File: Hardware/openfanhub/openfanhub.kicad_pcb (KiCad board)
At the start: 2 copper layers, 100 x 100 mm, 110 parts, among them J1 UART, J2 I2C, J3 12V in, J4 GND in, J5 5V IN, J6 SWD, M1 Fan_4pin, M10 Fan_4pin, M11 Fan_4pin, M12 Fan_4pin, M13 Fan_4pin, M14 Fan_4pin, M15 Fan_4pin, M16 Fan_4pin, M17 Fan_4pin, M18 Fan_4pin, M2 Fan_4pin, M3 Fan_4pin, M4 Fan_4pin, M5 Fan_4pin, M6 Fan_4pin, M7 Fan_4pin, M8 Fan_4pin, M9 Fan_4pin, Q1 Q_NMOS_GSD, Q10 AO449, Q11 Q_NMOS_GSD, Q12 AO449, Q2 AO449, Q3 Q_NMOS_GSD, Q4 AO449, Q5 Q_NMOS_GSD, Q6 AO449, Q7 Q_NMOS_GSD, Q8 AO449, Q9 Q_NMOS_GSD, U1 STM32F103C8T8_Board, U2 STM32F103C8Tx, U3 AMS1117, U4 AMS1117, U5 USB_HEADER_IN, U6 USB_HEADER_OUT, Y1 Crystal

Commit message: First pcb version
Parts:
- added C20: C_Polarized, Capacitor_THT:CP_Radial_D6.3mm_P2.50mm, F.Cu at (96.1, 79.6)
- added C21: C_Polarized, Capacitor_THT:CP_Radial_D6.3mm_P2.50mm, F.Cu at (117.1, 124.7)
- added C22: C_Polarized, Capacitor_THT:CP_Radial_D6.3mm_P2.50mm, F.Cu at (177.8, 61.9)
- added C23: C_Polarized, Capacitor_THT:CP_Radial_D6.3mm_P2.50mm, F.Cu at (178.0, 74.3)
- added C24: C_Polarized, Capacitor_THT:CP_Radial_D6.3mm_P2.50mm, F.Cu at (97.6, 65.4)
- added C25: C_Polarized, Capacitor_THT:CP_Radial_D6.3mm_P2.50mm, F.Cu at (183.5, 125.9)
- added JP4: 3Pin Jumper, Connector_PinHeader_2.54mm:PinHeader_1x02_P2.54mm_Vertical, F.Cu at (103.2, 77.6)
- added JP5: 3Pin Jumper, Connector_PinHeader_2.54mm:PinHeader_1x02_P2.54mm_Vertical, F.Cu at (96.9, 122.2)
- added JP6: 3Pin Jumper, Connector_PinHeader_2.54mm:PinHeader_1x02_P2.54mm_Vertical, F.Cu at (168.6, 60.9)
- added JP7: 3Pin Jumper, Connector_PinHeader_2.54mm:PinHeader_1x02_P2.54mm_Vertical, F.Cu at (178.0, 94.0)
- added JP8: 3Pin Jumper, Connector_PinHeader_2.54mm:PinHeader_1x02_P2.54mm_Vertical, F.Cu at (102.3, 61.4)
- added JP9: 3Pin Jumper, Connector_PinHeader_2.54mm:PinHeader_1x02_P2.54mm_Vertical, F.Cu at (160.2, 122.0)
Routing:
- net /FAN5_PWM: track 79.2 -> 91.5 mm
- net /FAN4_SWITCH: track 103.0 -> 113.9 mm, vias 4 -> 5
- net /FAN3_PWM: track 130.0 -> 140.9 mm
- net /FAN3_SWITCH: track 84.1 -> 94.8 mm, vias 2 -> 3
- net /FAN1_PWM: track 107.9 -> 115.5 mm
- net GND: track 32.0 -> 39.5 mm, vias 14 -> 15
- net /FAN5_SWITCH: track 43.9 -> 50.9 mm
- net /FAN6_SWITCH: track 68.9 -> 75.0 mm
- net /PWM_GROUPS/PWM_GROUP3/SWITCHED_POWER: track 36.0 -> 41.7 mm
- net /PWM_GROUPS/PWM_GROUP1/SWITCHED_POWER: track 35.7 -> 41.3 mm
- net /PWM_GROUPS/PWM_GROUP2/SWITCHED_POWER: track 35.7 -> 41.4 mm
- net /PWM_GROUPS/PWM_GROUP6/SWITCHED_POWER: track 36.1 -> 41.7 mm
- net /FAN1_SWITCH: track 118.7 -> 124.0 mm, vias 2 -> 3
- net /PWM_GROUPS/PWM_GROUP4/SWITCHED_POWER: track 36.1 -> 40.7 mm
- net /FAN2_SWITCH: track 78.3 -> 82.8 mm
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
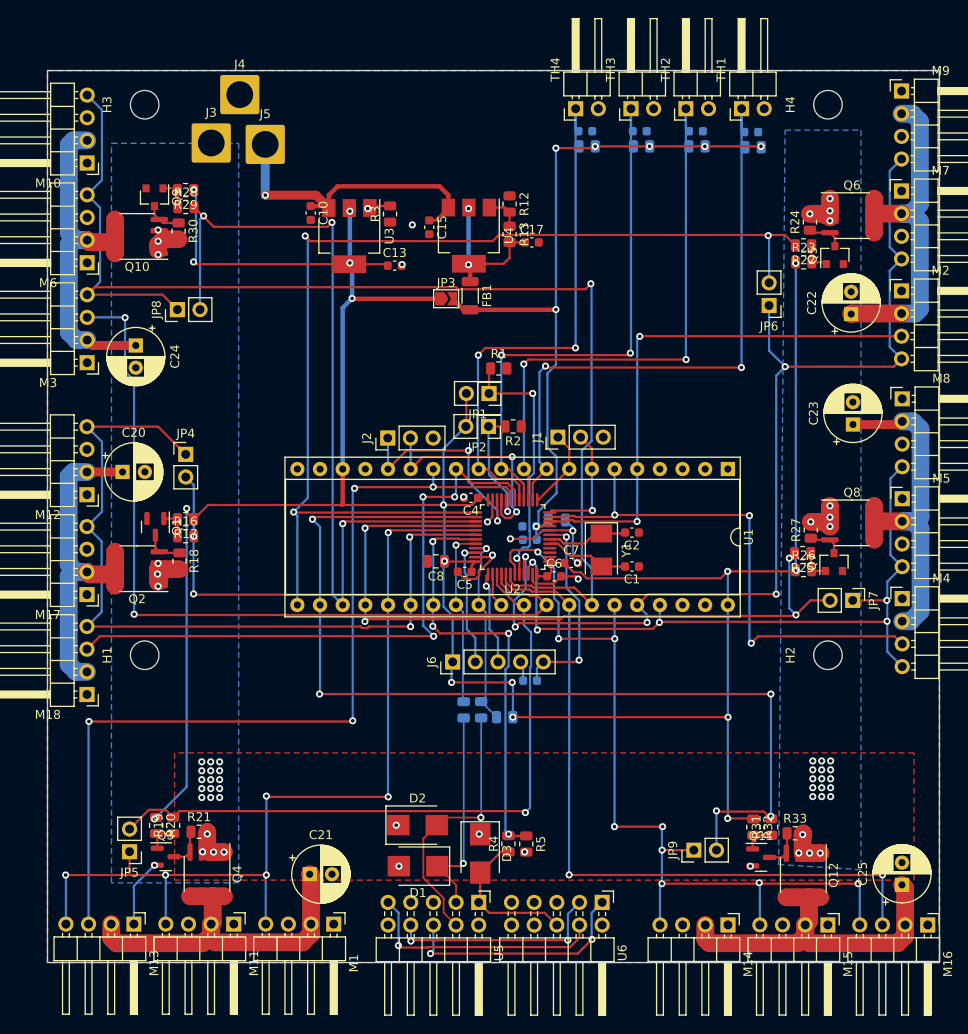
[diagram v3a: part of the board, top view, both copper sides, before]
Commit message: Update PCB. Move Power and USB to the same side
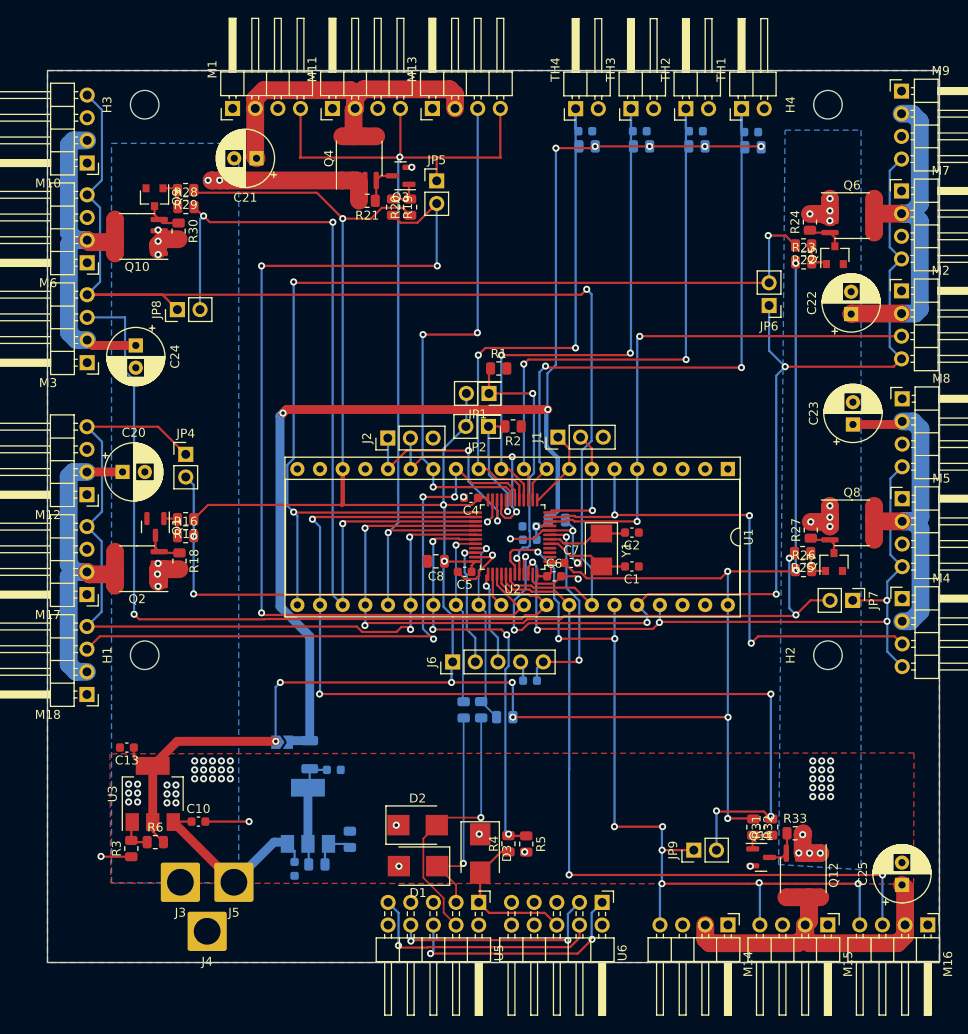
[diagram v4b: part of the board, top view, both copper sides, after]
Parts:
- C15, C17, FB1, JP3, R12, R13, U4: moved to B.Cu
- R6: moved to F.Cu
- moved M13 97.4 mm to (130.9, 38.8), turned to 90 degrees
- moved J4 93.9 mm to (105.6, 131.1), turned to 180 degrees
- moved M1 92.1 mm to (108.5, 38.8), turned to 90 degrees
- moved M11 92.1 mm to (119.7, 38.8), turned to 90 degrees
- moved J3 83.0 mm to (102.6, 125.6), turned to 180 degrees
- moved J5 82.8 mm to (108.6, 125.6), turned to 180 degrees
- moved JP5 82.7 mm to (131.3, 47.0), turned to 0 degrees
- moved Q4 82.0 mm to (122.7, 44.4), turned to 90 degrees
- moved Q3 80.8 mm to (127.3, 46.4), turned to 180 degrees
- moved C21 80.5 mm to (111.1, 44.4), turned to 180 degrees
- moved R3 76.8 mm to (97.1, 121.8)
- moved R20 74.9 mm to (128.4, 49.9), turned to 90 degrees
- moved R6 74.6 mm to (99.8, 121.1), turned to 0 degrees
- moved R13 73.9 mm to (117.9, 123.6), turned to 180 degrees
- moved R19 73.6 mm to (126.5, 49.9), turned to -90 degrees
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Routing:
- net +3.3VA: track 84.1 -> 141.2 mm, vias 7 -> 8
- net /FAN6_RPM: track 99.2 -> 58.8 mm, vias 4 -> 3
- net /FAN6_SWITCH: track 75.0 -> 106.9 mm, vias 1 -> 3
- net +12V: track 25.2 -> 39.9 mm, vias 52 -> 63
- net +5V: track 35.3 -> 22.0 mm, vias 1 -> 0
- net /FAN1_SWITCH: track 124.0 -> 119.6 mm
- net Net-(C17-Pad1): track 17.0 -> 12.8 mm, vias 2 -> 0
- net Net-(R3-Pad2): track 2.36 -> 3.96 mm, vias 1 -> 0
- net /FAN6_PWM: track 103.8 -> 102.3 mm, vias 6 -> 2
- net /FAN3_PWM: track 140.9 -> 139.6 mm
- net +3V3: track 316.5 -> 315.4 mm, vias 17 -> 13
- net Net-(R12-Pad2): track 4.05 -> 5.03 mm
- net /FAN5_PWM: track 91.5 -> 92.3 mm
- net GND: track 39.5 -> 40.3 mm
- net /FAN2_SWITCH: track 82.8 -> 83.4 mm
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
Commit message: Make PCB smaller
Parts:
- moved C25 6.02 mm to (183.0, 119.9)
- moved JP3 6.02 mm to (113.5, 103.9)
- moved R3 6.02 mm to (96.6, 115.8)
- moved U4 6.02 mm to (116.4, 112.1)
- moved M15 6.02 mm to (174.7, 124.4)
- moved Q12 6.02 mm to (171.9, 118.8)
- moved C10 6.02 mm to (104.1, 112.8)
- moved C13 6.02 mm to (96.1, 104.5)
- moved C15 6.02 mm to (114.9, 118.1)
- moved C17 6.02 mm to (119.3, 107.0)
- moved D1 6.02 mm to (128.8, 117.8)
- moved D2 6.02 mm to (128.7, 113.2)
- moved D3 6.02 mm to (135.7, 116.4)
- moved FB1 6.02 mm to (116.6, 105.3)
- moved J3 6.02 mm to (102.1, 119.6)
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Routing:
- net +3V3: track 315.4 -> 325.5 mm
- net /FAN4_PWM: track 99.3 -> 92.9 mm
- net /FAN4_RPM: track 80.1 -> 73.6 mm
- net +3.3VA: track 141.2 -> 135.0 mm
- net /VBUS_SENSE: track 48.3 -> 42.2 mm
- net /D1-: track 24.3 -> 18.5 mm
- net /D1+: track 29.8 -> 24.0 mm
- net /FAN4_SWITCH: track 113.9 -> 108.5 mm
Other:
- board size 100 x 100 mm -> 100 x 93.9 mm

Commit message: Update silkscreen
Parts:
- added REF**: OSHW-Symbol_13.4x12mm_SilkScreen, Symbol:OSHW-Symbol_13.4x12mm_SilkScreen, B.Cu at (119.2, 57.2)
- USB IN: renamed from U5
- USB OUT: renamed from U6
- renumbered J3 to 12V, J5 to 5V, J4 to GND
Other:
- board text added: "1"
- board text added: "2"
- board text added: "3"
- board text added: "4"
- board text added: "Fan 1"
- board text added: "Fan 2"
- board text added: "Fan 3"
- board text added: "Fan 4"
- board text added: "Fan 5"
- board text added: "Fan 6"
- board text added: "JLCJLCJLCJLC"
- board text added: "OpenFanHub v0.1"
- board text added: "Temperature input"

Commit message: Update (not sure what)
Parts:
- removed D1, D2, D3: D_TVS, Diode_SMD:D_SMB
- removed REF**: OSHW-Symbol_13.4x12mm_SilkScreen, Symbol:OSHW-Symbol_13.4x12mm_SilkScreen
- added U4: USBLC6-2SC6, Package_TO_SOT_SMD:SOT-23-6, B.Cu at (134.9, 115.3)
- Q1, Q11, Q3, Q5, Q7, Q9: value Q_NMOS_GSD -> IRLML2502
- Q10, Q12, Q2, Q4, Q6, Q8: value AO449 -> AO4409
- U6: renamed from USB IN
- U7: renamed from USB OUT
- moved R3 5.58 mm to (134.8, 111.5)
- moved R4 5.58 mm to (136.8, 111.5)
- renumbered 12V to J3, GND to J4, 5V to J5, R7 to R10, R4 to R3, R5 to R4, R3 to R5, R8 to R6, R6 to R7, R10 to R8, U4 to U5
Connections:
- R8 pad 2: /D1+ -> Net-(R8-Pad2)
- R9 pad 2: /D1- -> Net-(R9-Pad2)
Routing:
- net /D1+: track 24.0 -> 9.10 mm, vias 1 -> 0
- net /D1-: track 18.5 -> 5.77 mm, vias 1 -> 0
- net GND: track 40.3 -> 48.1 mm, vias 15 -> 26
- net Net-(R8-Pad2): track 0.00 -> 7.22 mm
- net Net-(R9-Pad2): track 0.00 -> 7.19 mm
- net /VBUS: track 17.3 -> 20.6 mm, vias 0 -> 1
- net Net-(U6-Pad6): track 26.7 -> 24.5 mm, vias 2 -> 1
- net Net-(U6-Pad9): track 27.6 -> 25.8 mm
- net /VBUS_SENSE: track 42.2 -> 40.5 mm
- net +3.3VA: track 135.0 -> 136.1 mm, vias 8 -> 9
- net Net-(U6-Pad8): track 24.2 -> 23.3 mm, vias 2 -> 1
- net /FAN1_RPM: track 60.2 -> 60.1 mm, vias 2 -> 4
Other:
- board text added: "12V"
- board text added: "5V"
- board text added: "GND"
- board text added: "TODO: Ground Path anschauen. Ist noch sehr eng Orientierung Fan Connectoren"

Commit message: update
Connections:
- M1 pad 1: GND -> /FAN6_PWM
- M1 pad 2: /PWM_GROUPS/PWM_GROUP6/SWITCHED_POWER -> /PWM_GROUPS/PWM_GROUP6/Subfan 2/RPM_OUT
- M1 pad 3: /PWM_GROUPS/PWM_GROUP6/Subfan 2/RPM_OUT -> /PWM_GROUPS/PWM_GROUP6/SWITCHED_POWER
- M1 pad 4: /FAN6_PWM -> GND
- M10 pad 1: GND -> /FAN3_PWM
- M10 pad 2: /PWM_GROUPS/PWM_GROUP3/SWITCHED_POWER -> /PWM_GROUPS/PWM_GROUP3/Subfan 3/RPM_OUT
- M10 pad 3: /PWM_GROUPS/PWM_GROUP3/Subfan 3/RPM_OUT -> /PWM_GROUPS/PWM_GROUP3/SWITCHED_POWER
- M10 pad 4: /FAN3_PWM -> GND
- M11 pad 1: GND -> /FAN6_PWM
- M11 pad 2: /PWM_GROUPS/PWM_GROUP6/SWITCHED_POWER -> /PWM_GROUPS/PWM_GROUP6/Subfan 3/RPM_OUT
- M11 pad 3: /PWM_GROUPS/PWM_GROUP6/Subfan 3/RPM_OUT -> /PWM_GROUPS/PWM_GROUP6/SWITCHED_POWER
- M11 pad 4: /FAN6_PWM -> GND
- M12 pad 1: GND -> /FAN5_PWM
- M12 pad 2: /PWM_GROUPS/PWM_GROUP5/SWITCHED_POWER -> /PWM_GROUPS/PWM_GROUP5/Subfan 2/RPM_OUT
- M12 pad 3: /PWM_GROUPS/PWM_GROUP5/Subfan 2/RPM_OUT -> /PWM_GROUPS/PWM_GROUP5/SWITCHED_POWER
- M12 pad 4: /FAN5_PWM -> GND
- M13 pad 1: GND -> /FAN6_PWM
- M13 pad 2: /PWM_GROUPS/PWM_GROUP6/SWITCHED_POWER -> /FAN6_RPM
- M13 pad 3: /FAN6_RPM -> /PWM_GROUPS/PWM_GROUP6/SWITCHED_POWER
- M13 pad 4: /FAN6_PWM -> GND
- M14 pad 1: GND -> /FAN4_PWM
- M14 pad 2: /PWM_GROUPS/PWM_GROUP4/SWITCHED_POWER -> /PWM_GROUPS/PWM_GROUP4/Subfan 2/RPM_OUT
- M14 pad 3: /PWM_GROUPS/PWM_GROUP4/Subfan 2/RPM_OUT -> /PWM_GROUPS/PWM_GROUP4/SWITCHED_POWER
- M14 pad 4: /FAN4_PWM -> GND
- M15 pad 1: GND -> /FAN4_PWM
- M15 pad 2: /PWM_GROUPS/PWM_GROUP4/SWITCHED_POWER -> /PWM_GROUPS/PWM_GROUP4/Subfan 3/RPM_OUT
- M15 pad 3: /PWM_GROUPS/PWM_GROUP4/Subfan 3/RPM_OUT -> /PWM_GROUPS/PWM_GROUP4/SWITCHED_POWER
- M15 pad 4: /FAN4_PWM -> GND
- M16 pad 1: GND -> /FAN4_PWM
- M16 pad 2: /PWM_GROUPS/PWM_GROUP4/SWITCHED_POWER -> /FAN4_RPM
- M16 pad 3: /FAN4_RPM -> /PWM_GROUPS/PWM_GROUP4/SWITCHED_POWER
- M16 pad 4: /FAN4_PWM -> GND
- M17 pad 1: GND -> /FAN5_PWM
- M17 pad 2: /PWM_GROUPS/PWM_GROUP5/SWITCHED_POWER -> /PWM_GROUPS/PWM_GROUP5/Subfan 3/RPM_OUT
- M17 pad 3: /PWM_GROUPS/PWM_GROUP5/Subfan 3/RPM_OUT -> /PWM_GROUPS/PWM_GROUP5/SWITCHED_POWER
- M17 pad 4: /FAN5_PWM -> GND
- M18 pad 1: GND -> /FAN5_PWM
- M18 pad 2: /PWM_GROUPS/PWM_GROUP5/SWITCHED_POWER -> /FAN5_RPM
- M18 pad 3: /FAN5_RPM -> /PWM_GROUPS/PWM_GROUP5/SWITCHED_POWER
- M18 pad 4: /FAN5_PWM -> GND
- M2 pad 1: GND -> /FAN1_PWM
- M2 pad 2: /PWM_GROUPS/PWM_GROUP1/SWITCHED_POWER -> /FAN1_RPM
- M2 pad 3: /FAN1_RPM -> /PWM_GROUPS/PWM_GROUP1/SWITCHED_POWER
- M2 pad 4: /FAN1_PWM -> GND
- M3 pad 1: GND -> /FAN3_PWM
- M3 pad 2: /PWM_GROUPS/PWM_GROUP3/SWITCHED_POWER -> /FAN3_RPM
- M3 pad 3: /FAN3_RPM -> /PWM_GROUPS/PWM_GROUP3/SWITCHED_POWER
- M3 pad 4: /FAN3_PWM -> GND
- M4 pad 1: GND -> /FAN2_PWM
- M4 pad 2: /PWM_GROUPS/PWM_GROUP2/SWITCHED_POWER -> /FAN2_RPM
- M4 pad 3: /FAN2_RPM -> /PWM_GROUPS/PWM_GROUP2/SWITCHED_POWER
- M4 pad 4: /FAN2_PWM -> GND
- M5 pad 1: GND -> /FAN2_PWM
- M5 pad 2: /PWM_GROUPS/PWM_GROUP2/SWITCHED_POWER -> /PWM_GROUPS/PWM_GROUP2/Subfan 2/RPM_OUT
- M5 pad 3: /PWM_GROUPS/PWM_GROUP2/Subfan 2/RPM_OUT -> /PWM_GROUPS/PWM_GROUP2/SWITCHED_POWER
- M5 pad 4: /FAN2_PWM -> GND
- M6 pad 1: GND -> /FAN3_PWM
- M6 pad 2: /PWM_GROUPS/PWM_GROUP3/SWITCHED_POWER -> /PWM_GROUPS/PWM_GROUP3/Subfan 2/RPM_OUT
- M6 pad 3: /PWM_GROUPS/PWM_GROUP3/Subfan 2/RPM_OUT -> /PWM_GROUPS/PWM_GROUP3/SWITCHED_POWER
- M6 pad 4: /FAN3_PWM -> GND
- M7 pad 1: GND -> /FAN1_PWM
- M7 pad 2: /PWM_GROUPS/PWM_GROUP1/SWITCHED_POWER -> /PWM_GROUPS/PWM_GROUP1/Subfan 2/RPM_OUT
- M7 pad 3: /PWM_GROUPS/PWM_GROUP1/Subfan 2/RPM_OUT -> /PWM_GROUPS/PWM_GROUP1/SWITCHED_POWER
- M7 pad 4: /FAN1_PWM -> GND
- M8 pad 1: GND -> /FAN2_PWM
- M8 pad 2: /PWM_GROUPS/PWM_GROUP2/SWITCHED_POWER -> /PWM_GROUPS/PWM_GROUP2/Subfan 3/RPM_OUT
- M8 pad 3: /PWM_GROUPS/PWM_GROUP2/Subfan 3/RPM_OUT -> /PWM_GROUPS/PWM_GROUP2/SWITCHED_POWER
- M8 pad 4: /FAN2_PWM -> GND
- M9 pad 1: GND -> /FAN1_PWM
- M9 pad 2: /PWM_GROUPS/PWM_GROUP1/SWITCHED_POWER -> /PWM_GROUPS/PWM_GROUP1/Subfan 3/RPM_OUT
- M9 pad 3: /PWM_GROUPS/PWM_GROUP1/Subfan 3/RPM_OUT -> /PWM_GROUPS/PWM_GROUP1/SWITCHED_POWER
- M9 pad 4: /FAN1_PWM -> GND
- U6 pad 2: GND -> Net-(U6-Pad2)
- U6 pad 4: /D1+ -> Net-(U6-Pad4)
- U6 pad 5: unconnected-(U6-Pad5) -> /D1+
- U6 pad 8: Net-(U6-Pad8) -> GND
- U6 pad 9: Net-(U6-Pad9) -> unconnected-(U6-Pad9)
- U7 pad 1: Net-(U6-Pad6) -> Net-(U6-Pad2)
- U7 pad 2: GND -> /VBUS
- U7 pad 3: Net-(U6-Pad8) -> Net-(U6-Pad4)
- U7 pad 4: Net-(U6-Pad9) -> unconnected-(U7-Pad4)
- U7 pad 5: unconnected-(U7-Pad5) -> Net-(U6-Pad6)
- U7 pad 6: /VBUS -> unconnected-(U7-Pad6)
- U7 pad 8: unconnected-(U7-Pad8) -> GND
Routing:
- net /FAN5_PWM: track 92.3 -> 27.3 mm, vias 2 -> 1
- net /FAN3_PWM: track 139.1 -> 93.9 mm
- net /FAN1_PWM: track 116.1 -> 77.3 mm, vias 5 -> 4
- net /PWM_GROUPS/PWM_GROUP3/SWITCHED_POWER: track 41.7 -> 3.81 mm
- net /PWM_GROUPS/PWM_GROUP6/SWITCHED_POWER: track 41.7 -> 3.81 mm
- net /PWM_GROUPS/PWM_GROUP1/SWITCHED_POWER: track 41.3 -> 4.04 mm
- net /PWM_GROUPS/PWM_GROUP2/SWITCHED_POWER: track 41.4 -> 4.15 mm
- net /PWM_GROUPS/PWM_GROUP4/SWITCHED_POWER: track 40.7 -> 3.81 mm
- net /PWM_GROUPS/PWM_GROUP5/SWITCHED_POWER: track 40.1 -> 3.81 mm
- net Net-(U6-Pad9): track 25.8 -> 0.00 mm, vias 1 -> 0
- net /FAN2_PWM: track 79.7 -> 54.3 mm, vias 5 -> 4
- net Net-(U6-Pad2): track 0.00 -> 23.7 mm, vias 0 -> 3
- net Net-(U6-Pad8): track 23.3 -> 0.00 mm, vias 1 -> 0
- net Net-(U6-Pad4): track 0.00 -> 16.4 mm
- net Net-(U6-Pad6): track 24.5 -> 14.9 mm, vias 1 -> 0
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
